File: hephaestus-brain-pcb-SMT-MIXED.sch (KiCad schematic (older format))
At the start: 35 parts, among them IC1 ATSAMD51G19A-MU, J1 Barrel_Jack, J2 Conn_02x03_Odd_Even, J3 StemmaQT, J4 Conn_01x03_Female, J5 Conn_01x03_Male, J6 Conn_01x03_Male, J7 Conn_01x03_Male, J8 USB4110-GF-A, SW1 SW_SPDT, SW2 SW_SPST, SW3 SW_SPST, U1 LM1117-5.0, U2 AP2112K-3.3, U3 AT25xxx-MA, U4 74LVC1G125

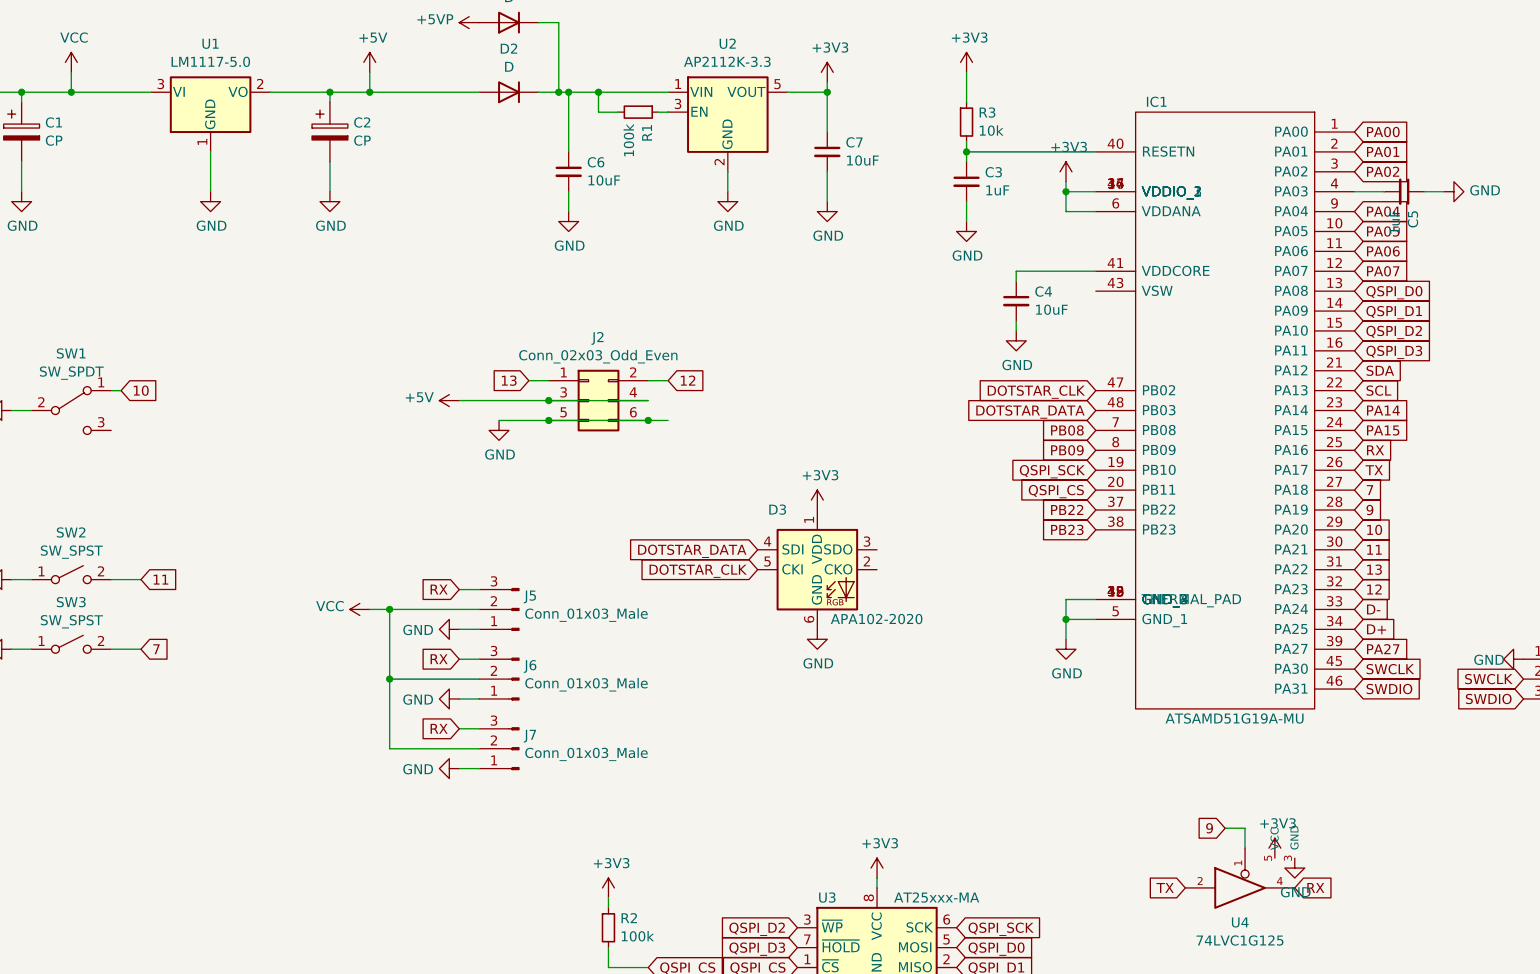
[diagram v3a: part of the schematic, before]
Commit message: Updated footprints.
0.22mm soldermask clearence on the USB and flash ICs
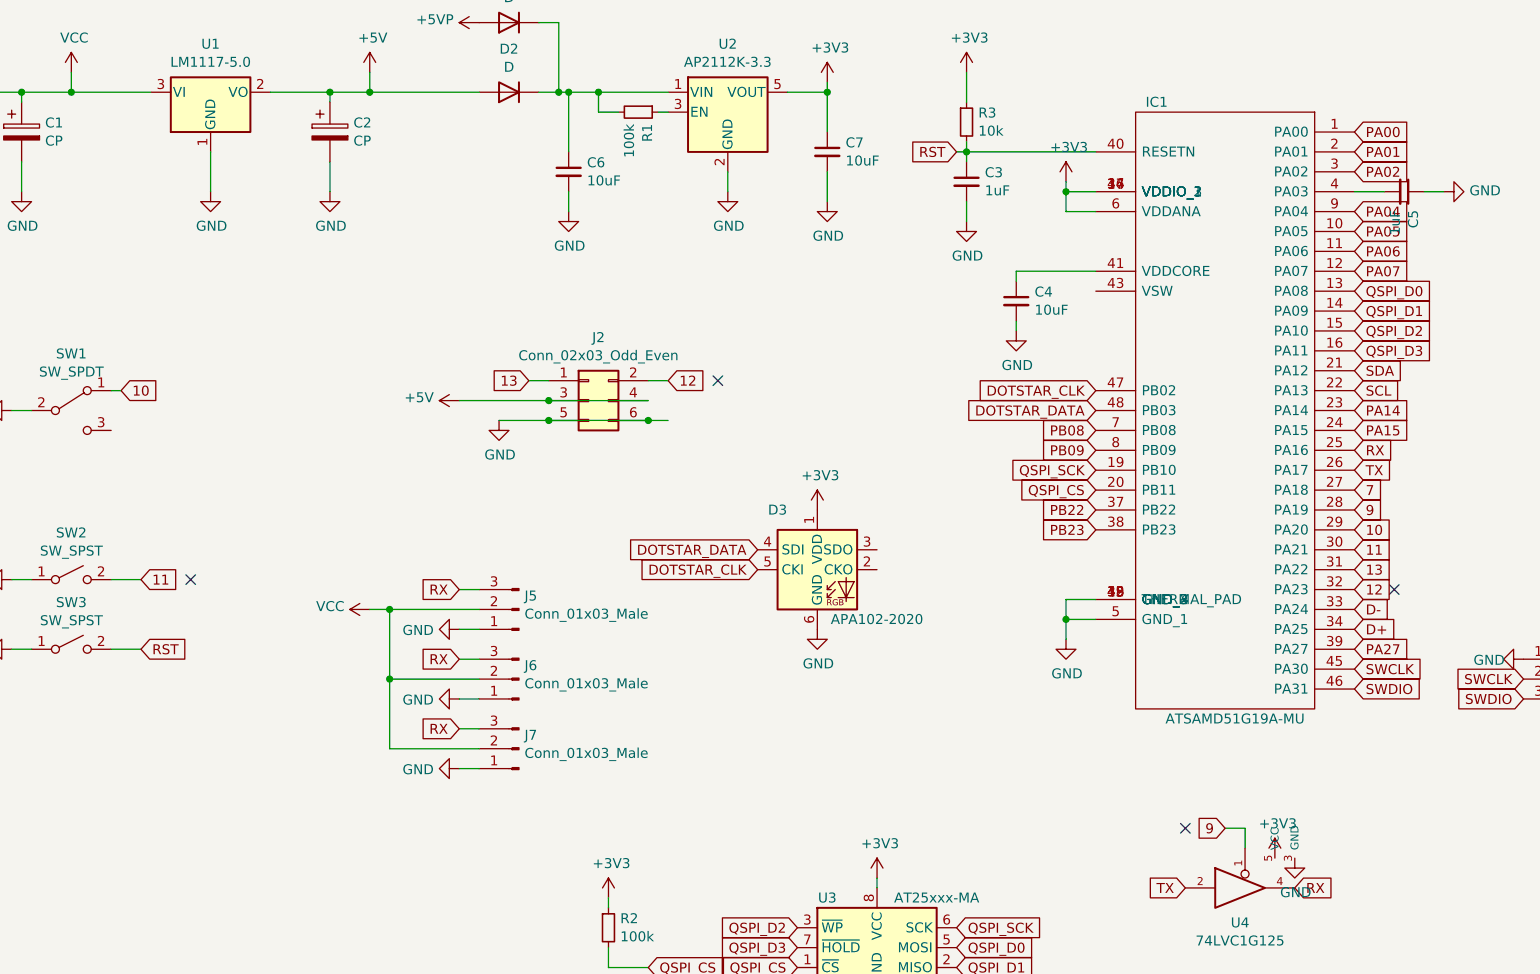
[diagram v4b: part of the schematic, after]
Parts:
- D3: footprint LED_SMD:LED-APA102-2020 -> unified:LED-APA102-2020
- J1: footprint Connector_BarrelJack:BarrelJack_CUI_PJ-102AH_Horizontal -> Connector_BarrelJack:BarrelJack_Wuerth_6941xx301002
- U3: footprint Package_DFN_QFN:DFN-8-1EP_3x2mm_P0.5mm_EP1.75x1.45mm -> unified:DFN-8-1EP_3x2mm_P0.5mm_EP1.75x1.45mm
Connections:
- net 7: no longer SW3.2 (B)
- net RST: now reaches C3.1, IC1.40 (RESETN), R3.2
- net RST: now also SW3.2 (B)
- no-connect marks 0 -> 4
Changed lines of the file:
@@
 F 0 "J1" H 1457 1975 50  0000 C CNN
 F 1 "Barrel_Jack" H 1457 1884 50  0000 C CNN
-F 2 "Connector_BarrelJack:BarrelJack_CUI_PJ-102AH_Horizontal" H 1450 1610 50  0001 C CNN
+F 2 "Connector_BarrelJack:BarrelJack_Wuerth_6941xx301002" H 1450 1610 50  0001 C CNN
 F 3 "PJ-102AH" H 1450 1610 50  0001 C CNN
 F 4 "DC-005-5A-2.0-SMT" H 1400 1650 50  0001 C CNN "mpn"
@@
 F 0 "U3" H 6500 6100 50  0000 C CNN
 F 1 "AT25xxx-MA" H 7050 6100 50  0000 C CNN
-F 2 "Package_DFN_QFN:DFN-8-1EP_3x2mm_P0.5mm_EP1.75x1.45mm" H 6750 5850 50  0001 C CNN
+F 2 "unified:DFN-8-1EP_3x2mm_P0.5mm_EP1.75x1.45mm" H 6750 5850 50  0001 C CNN
 F 3 "http://ww1.microchip.com/downloads/en/DeviceDoc/Atmel-8707-SEEPROM-AT25010B-020B-040B-Datasheet.pdf" H 6750 5850 50  0001 C CNN
 	1    6750 5850
@@
 F 0 "D3" H 6250 4250 50  0000 C CNN
 F 1 "APA102-2020" H 6750 3700 50  0000 C CNN
-F 2 "LED_SMD:LED-APA102-2020" H 6500 3650 50  0001 L TNN
+F 2 "unified:LED-APA102-2020" H 6500 3650 50  0001 L TNN
 F 3 "http://www.led-color.com/upload/201604/APA102-2020%20SMD%20LED.pdf" H 6550 3575 50  0001 L TNN
 	1    6450 3950
@@
 $EndComp
 Text GLabel 9150 3550 2    50   Input ~ 0
-7
-Text GLabel 3050 4350 2    50   Input ~ 0
 7
 Text GLabel 9150 3250 2    50   Input ~ 0
@@
 Text GLabel 10000 4500 0    50   Input ~ 0
 SWCLK
+NoConn ~ 5950 3000
+NoConn ~ 9350 4050
+NoConn ~ 3300 4000
+NoConn ~ 8300 5250
+Text GLabel 7150 1850 0    50   Input ~ 0
+RST
+Wire Wire Line
+	7200 1850 7150 1850
+Text GLabel 3050 4350 2    50   Input ~ 0
+RST
 $EndSCHEMATC
